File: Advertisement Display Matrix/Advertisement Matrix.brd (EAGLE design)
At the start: 94.6 x 64.1 mm, 27 parts, among them IC1 MAX7219CNG, IC2 74HC540N, IC3 UDN2981A, IC9 ATMEGA168-20P, Y3 16Mhz

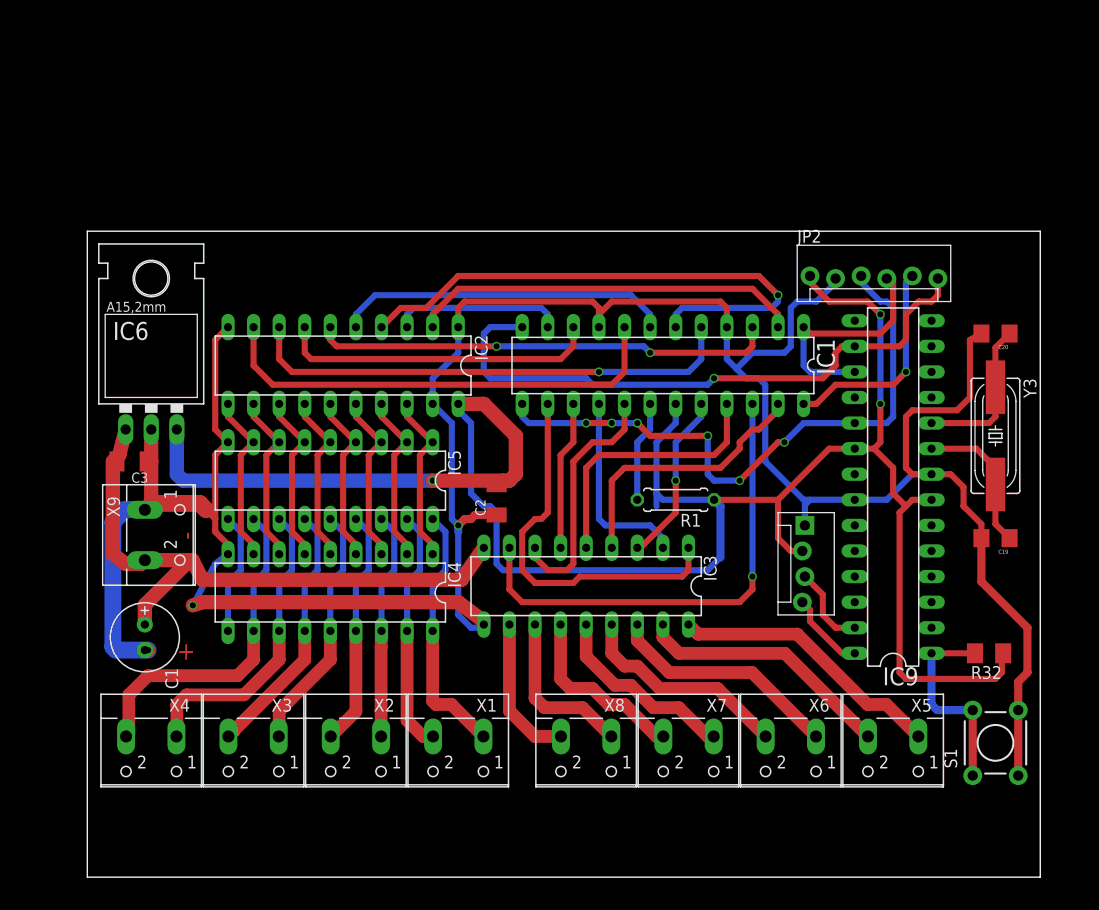
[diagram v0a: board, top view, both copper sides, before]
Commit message: Tiny-TinyG, Plus gerbers of Reflow and Advertisement
Started new project: TinyTinyG
Generated Gerbers for Advertisement Display driver and ReflowOvenShield
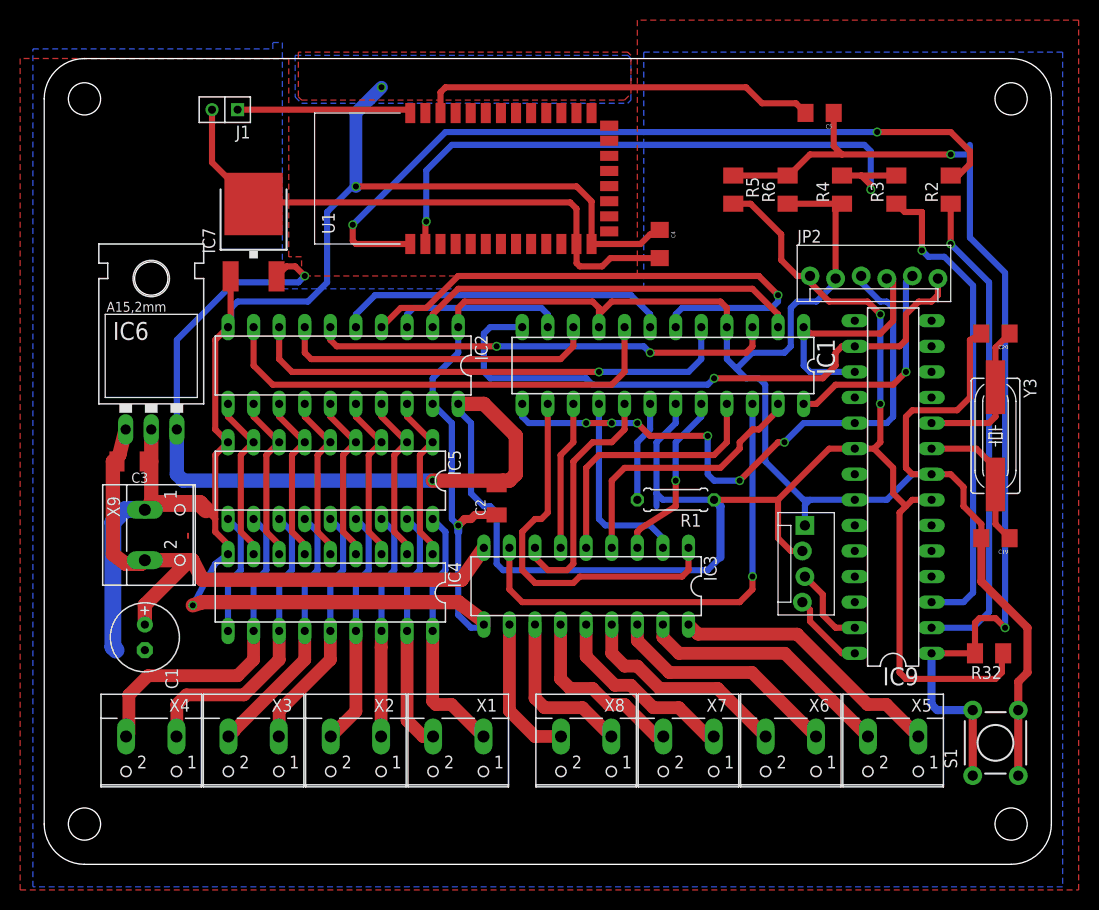
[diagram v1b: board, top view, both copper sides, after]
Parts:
- added C4, C5: 100u, SparkFun-Passives:1206
- added IC7: V-REG_LD117ADT-TR, untitled:V-REG_DPACK
- added J1: CON_HEADER_1X02-PTH, dp_devices:M1X2
- added PCB1: PCB_DP_RECTANGLE-80X100, dp_devices:DP10080_V1
- added R2: 10R, resistor:M1206
- added R3, R5: 10k, resistor:M1206
- added R4, R6: 15K, resistor:M1206
- added U1: SERIALPORTBLUETOOTH_HC_05, untitled:SERIALPORTBLUETOOTH_BLUETOOTH_SMD
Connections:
- removed net LCDRESET: IC9.1, R32.2, S1.1, S1.2
- new net 3V3: C4.2, IC7.4, J1.2, U1.12
- new net ATRX: IC9.2, R2.1
- new net ATTX: IC9.3, R3.1
- new net N$43: R2.2, U1.1
- new net N$44: R3.2, R4.2, U1.2
- new net N$45: J1.1, U1.34
- new net N$47: C5.2, U1.32
- new net RESET: C5.1, IC9.1, R32.2, R5.1, R6.2, S1.1, S1.2
- net GND: now also C4.1, IC7.1, R4.1, R6.1, U1.13
- net VCC: now also IC7.3, R5.2
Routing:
- net RESET: track 0.00 -> 105.0 mm, vias 0 -> 2
- net GND: track 280.5 -> 365.2 mm, vias 3 -> 4
- net N$43: track 0.00 -> 77.0 mm, vias 0 -> 2
- net N$44: track 0.00 -> 63.8 mm, vias 0 -> 2
- net 3V3: track 0.00 -> 57.6 mm
- net ATRX: track 0.00 -> 48.5 mm, vias 0 -> 1
- net ATTX: track 0.00 -> 48.2 mm, vias 0 -> 1
- net VCC: track 200.5 -> 240.4 mm, vias 3 -> 4
- net N$47: track 0.00 -> 39.6 mm
- net LCDRESET: track 20.2 -> 0.00 mm
- net N$45: track 0.00 -> 17.3 mm
- added copper zone on layer 1, net GND
- added copper zone on layer 16, net GND
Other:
- board size 94.6 x 64.1 mm -> 100 x 80 mm
- board text added: "10-R"
- board text added: "104\"
- board text added: "1117-3.3"
- board text added: "12V LED Matrix Driver"
- board text added: "12V-IN"
- board text added: "15K"
- board text added: "BLUETOOTH"
- board text added: "BT-KEY-3.3"
- board text added: "OPENHARDWARE.CO.ZA"
- board text added: "with Bluetooth"
